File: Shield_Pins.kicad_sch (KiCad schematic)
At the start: 0 parts

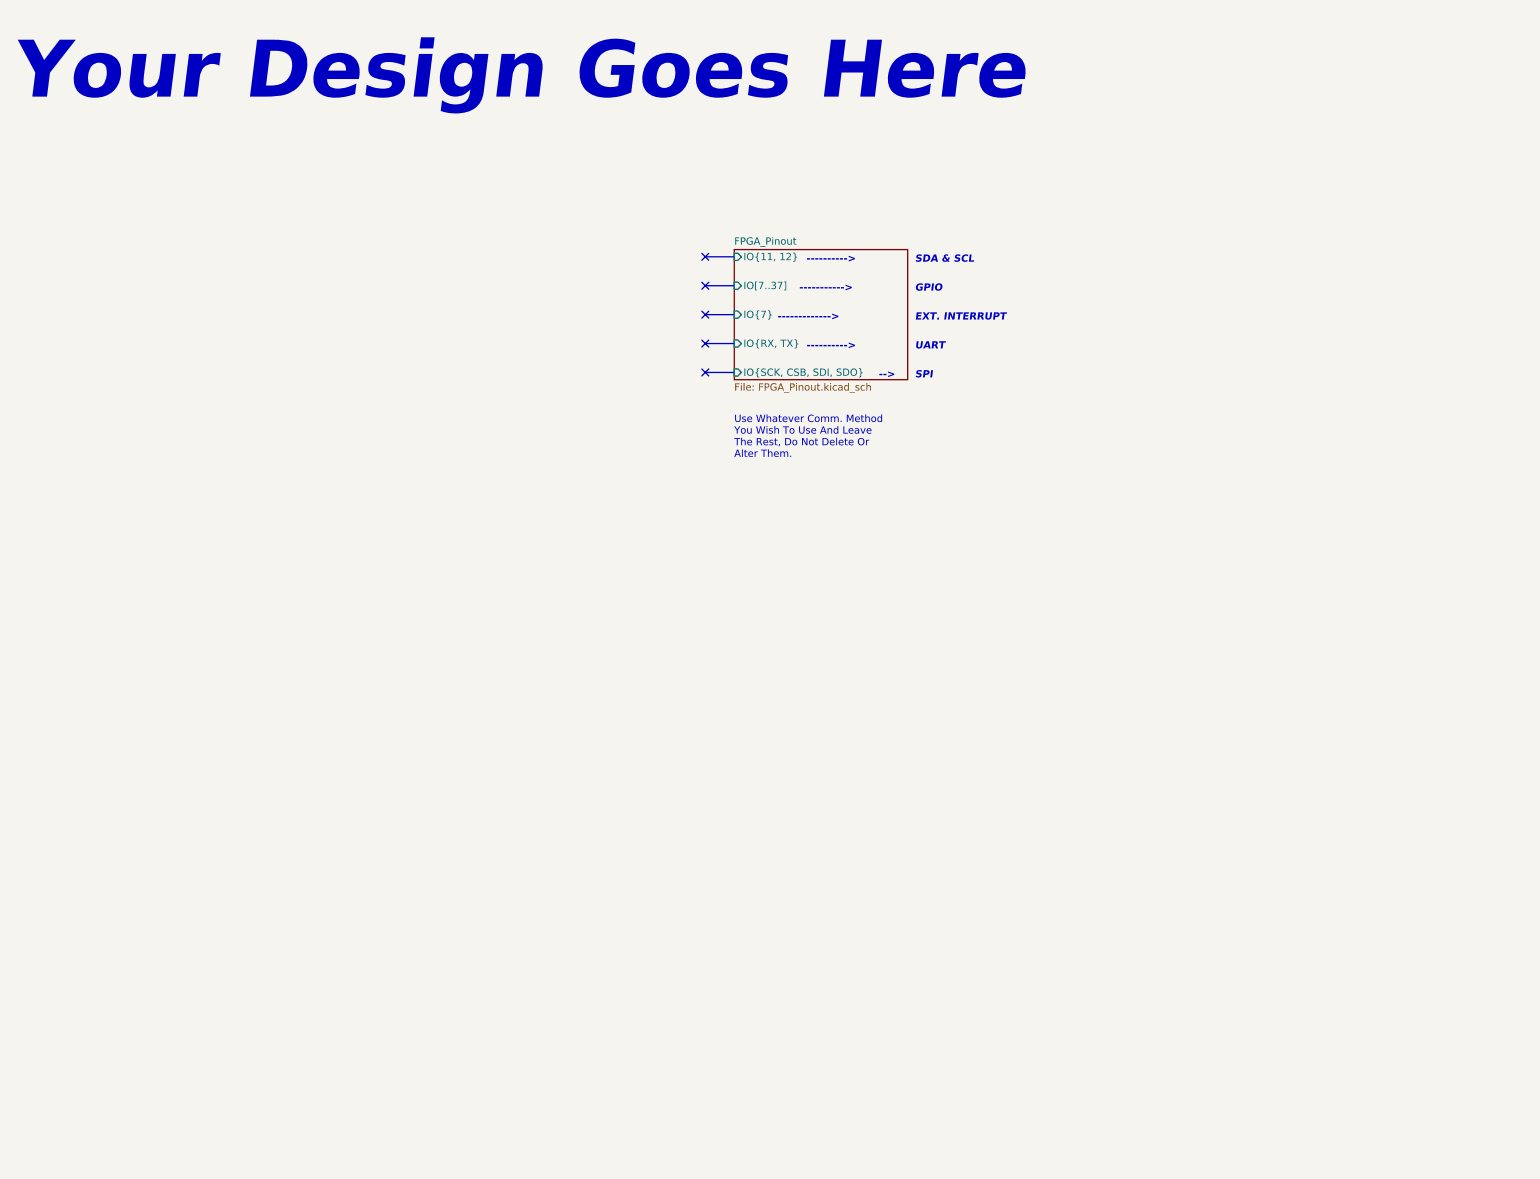
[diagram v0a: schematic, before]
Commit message: First commit: GPS Shield Schematic Progress
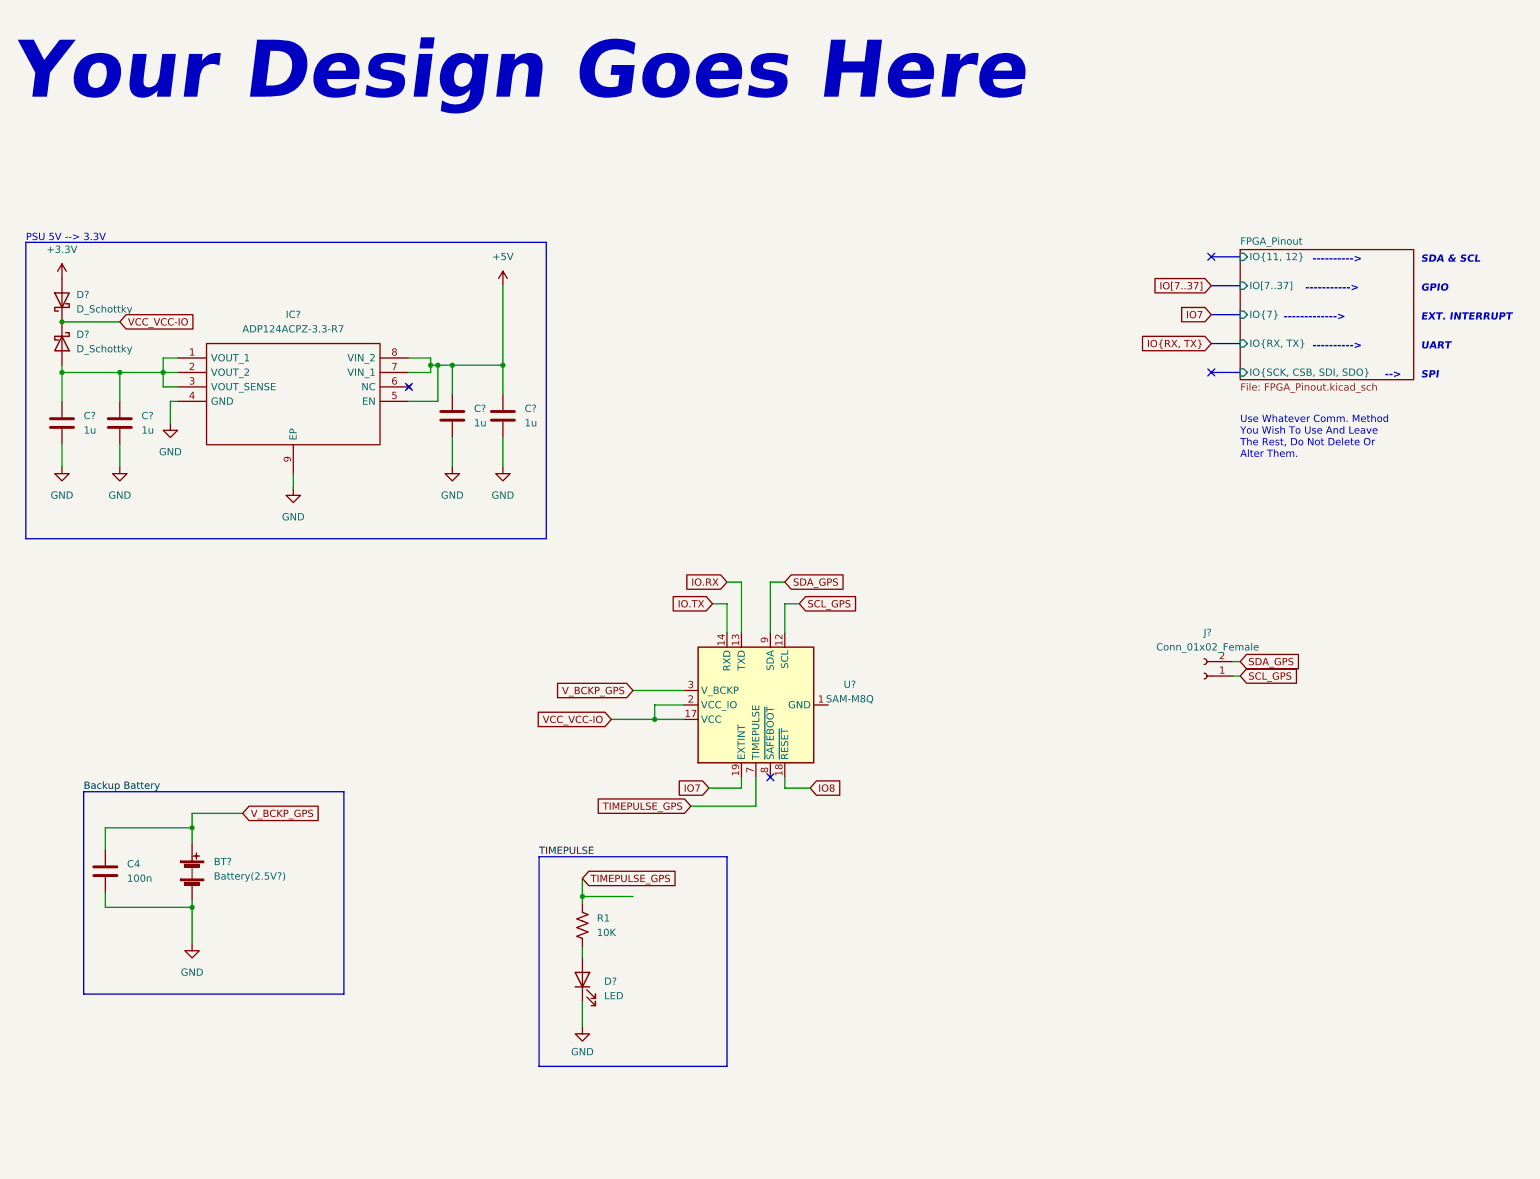
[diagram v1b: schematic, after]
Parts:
- added BT?: Battery(2.5V?), symbol Device:Battery
- added C4: 100n, symbol Device:C
- added C? (x4): 1u, symbol Device:C
- added D? (x2): D_Schottky, symbol Device:D_Schottky
- added D?: LED, symbol Device:LED
- added IC?: ADP124ACPZ-3.3-R7, SON50P200X200X65-9N-D, symbol Regulator_Linear:ADP124ACPZ-3.3-R7
- added J?: Conn_01x02_Female, symbol Connector:Conn_01x02_Female
- added R1: 10K, symbol Device:R_US
- added U?: SAM-M8Q, RF_GPS:ublox_SAM-M8Q, symbol RF_GPS:SAM-M8Q
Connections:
- new net: D?.2 (A), R1.1
- new net: C?.1, C?.1, D?.2 (A), IC?.1 (VOUT_1), IC?.2 (VOUT_2), IC?.3 (VOUT_SENSE)
- new net: U?.1 (GND), U?.10 (GND), U?.11 (GND), U?.15 (GND), U?.16 (GND), U?.20 (GND), U?.4 (GND), U?.5 (GND), U?.6 (GND)
- new net +3.3V: D?.2 (A)
- new net +5V: C?.1, C?.1, IC?.5 (EN), IC?.7 (VIN_1), IC?.8 (VIN_2)
- new net GND: BT?.2 (-), C4.2, C?.2, C?.2, C?.2, C?.2, D?.1 (K), IC?.4 (GND), IC?.9 (EP)
- new net IO.RX: U?.13 (TXD)
- new net IO.TX: U?.14 (RXD)
- new net IO7: U?.19 (EXTINT)
- new net IO8: U?.18 (~{RESET})
- new net SCL_GPS: J?.1 (Pin_1), U?.12 (SCL)
- new net SDA_GPS: J?.2 (Pin_2), U?.9 (SDA)
- new net TIMEPULSE_GPS: R1.2, U?.7 (TIMEPULSE)
- new net VCC_VCC-IO: D?.1 (K), D?.1 (K), U?.17 (VCC), U?.2 (VCC_IO)
- new net V_BCKP_GPS: BT?.1 (+), C4.1, U?.3 (V_BCKP)
- no-connect marks 5 -> 4
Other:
- note added: "PSU 5V --> 3.3V"

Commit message: First Shield Commit
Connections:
- net TIMEPULSE_GPS renamed IO9
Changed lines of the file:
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@@
+    )
+  )
+  (global_label "IO9" (shape input) (at 127 133.985 0) (fields_autoplaced)
+    (effects (font (size 1.27 1.27)) (justify left))
+    (property "Intersheet References" "${INTERSHEET_REFS}" (id 0) (at 132.5579 133.9056 0)
+      (effects (font (size 1.27 1.27)) (justify left) hide)
     )
   )

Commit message: Add files via upload
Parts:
- removed D?: D_Schottky, symbol Device:D_Schottky
- added D3, D4, D5, D6, D7: LED, Diode_SMD:D_1206_3216Metric, symbol Device:LED
- added D8: D_Schottky, Diode_SMD:D_1206_3216Metric, symbol Device:D_Schottky
- added J11: Conn_01x02_Female, Connector_PinHeader_2.00mm:PinHeader_1x02_P2.00mm_Vertical, symbol Connector:Conn_01x02_Female
- added Q1, Q2: QNPN, Package_TO_SOT_SMD:SOT-23-8, symbol pspice:QNPN
- added R2: 330, Resistor_SMD:R_1206_3216Metric, symbol Device:R_US
- added R3, R6: 150, Resistor_SMD:R_1206_3216Metric, symbol Device:R_US
- added R4: 170, Resistor_SMD:R_1206_3216Metric, symbol Device:R_US
- added R5: 130, Resistor_SMD:R_1206_3216Metric, symbol Device:R_US
- BT1: renamed from BT?; footprint (none) -> Battery:BatteryHolder_Keystone_2998_1x6.8mm
- C1, C2, C3, C5: renamed from C?; footprint (none) -> Capacitor_SMD:C_1206_3216Metric
- C4: footprint (none) -> Capacitor_SMD:C_1206_3216Metric
- D1, D2: renamed from D?; footprint (none) -> Diode_SMD:D_1206_3216Metric
- IC1: renamed from IC?; footprint SON50P200X200X65-9N-D -> Package_SON:SON50P200X200X60-9N
- J10: renamed from J?; footprint (none) -> Connector_PinHeader_2.00mm:PinHeader_1x02_P2.00mm_Vertical
- R1: value 10K -> 170; footprint (none) -> Resistor_SMD:R_1206_3216Metric
- gave numbers to parts that had none: 1
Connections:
- net IO7 is gone; now on net IO9: U1.19 (EXTINT)
- net VCC_VCC-IO is gone; now on net +3.3V: D1.1 (K), U1.17 (VCC), U1.2 (VCC_IO)
- net +3.3V: now also R1.2, D8.2 (A), R3.1, R4.2, R6.1
- net +5V: now also R2.2
- net GND: now also U1.1 (GND), U1.10 (GND), U1.11 (GND), U1.15 (GND), U1.16 (GND), U1.20 (GND), U1.4 (GND), U1.5 (GND), U1.6 (GND), D3.1 (K), D5.1 (K), D6.1 (K), Q1.3 (E), Q1.4 (Substrat), Q2.3 (E)
- net IO.RX: now also U1.14 (RXD), J11.2 (Pin_2); no longer U1.13 (TXD)
- net IO.TX: now also U1.13 (TXD), J11.1 (Pin_1); no longer U1.14 (RXD)
- net IO9: no longer R1.2, U1.7 (TIMEPULSE)
- net V_BCKP_GPS: now also R5.2
- net IO22: now reaches U1.8 (~{SAFEBOOT})
- new net: D6.2 (A), R5.1
- new net: D7.2 (A), R6.2
- new net: D4.1 (K), Q1.1 (C)
- new net: D4.2 (A), R3.2
- new net: D5.2 (A), R4.1
- new net: D3.2 (A), R2.1
- new net IO.RX_LED: Q1.2 (B)
- new net IO.TX_LED: Q2.2 (B)
- new net TIMEPULSE_GPS: D8.1 (K), U1.7 (TIMEPULSE)
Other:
- sheet FPGA_Pinout ports: added F{IO0, IO1, CLK, CSB}; removed none
- note added: "Backup Battery"
- note added: "Connections"
- note added: "LEDs"
- note added: "SAM-M8Q"
- note added: "TIMEPULSE"
- moved on the sheet: BT1, C4, D2, J10, R1, U1

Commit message: Add files via upload
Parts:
- removed Q1, Q2: QNPN, Package_TO_SOT_SMD:SOT-23-8, symbol pspice:QNPN
- added C6: 1u, Capacitor_SMD:C_1206_3216Metric, symbol Device:C
- added Q1, Q2: 2N2219, Package_TO_SOT_SMD:SOT-23, symbol Transistor_BJT:2N2219
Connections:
- net +3.3V: now also C6.1
- net GND: now also C6.2, Q1.1 (E), Q2.1 (E)
- net IO.RX: now also Q1.2 (B)
- net IO.TX: now also Q2.2 (B)
- net at D4.1 (K): now also Q1.3 (C)
- net at D7.1 (K): now also Q2.3 (C)
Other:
- moved on the sheet: D4, R3
